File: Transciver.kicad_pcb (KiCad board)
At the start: 2 copper layers, 4 parts, among them SW1 SW_DIP_x02

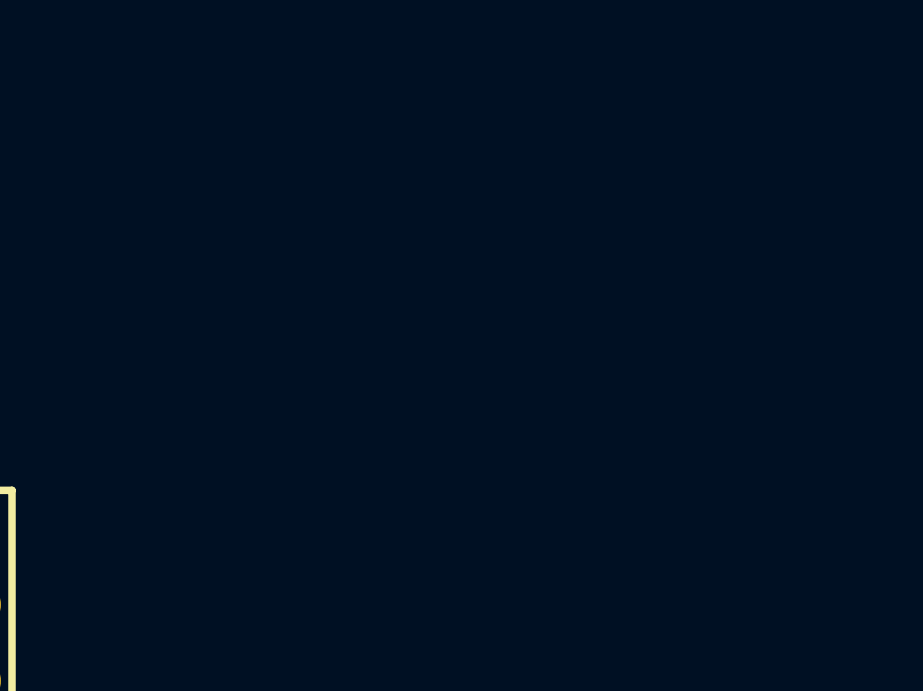
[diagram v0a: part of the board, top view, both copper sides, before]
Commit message: Debug Led and Resistor added
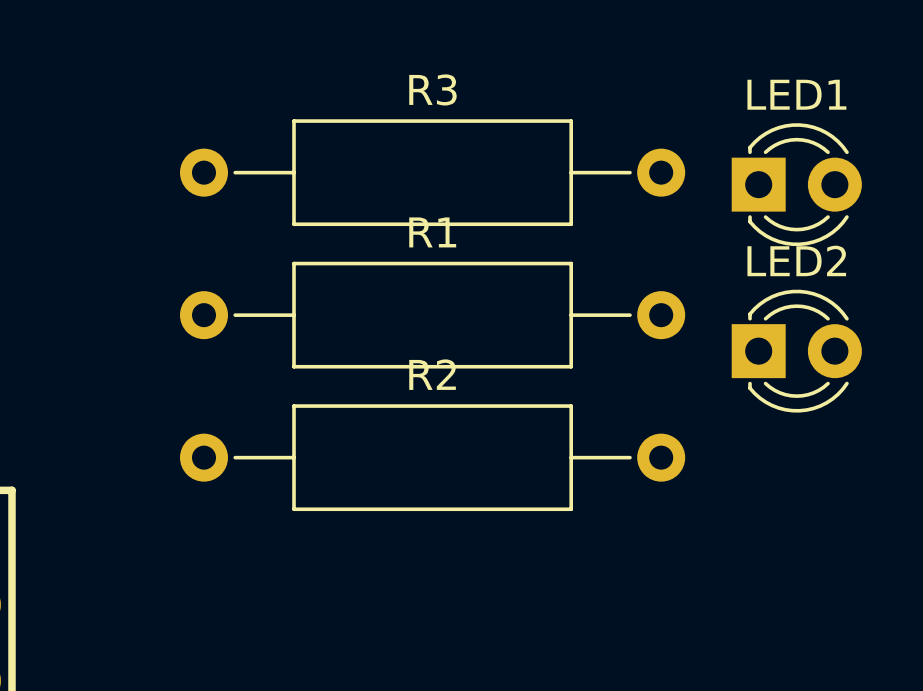
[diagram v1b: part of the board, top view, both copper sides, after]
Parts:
- added LED1: LED, LED_THT:LED_D3.0mm, F.Cu at (121.2, 31.8)
- added LED2: LED, LED_THT:LED_D3.0mm, F.Cu at (121.2, 37.4)
- added R1: 220K, Resistor_THT:R_Axial_DIN0309_L9.0mm_D3.2mm_P15.24mm_Horizontal, F.Cu at (102.7, 36.1)
- added R2: 10K, Resistor_THT:R_Axial_DIN0309_L9.0mm_D3.2mm_P15.24mm_Horizontal, F.Cu at (102.7, 40.9)
- added R3: 220K, Resistor_THT:R_Axial_DIN0309_L9.0mm_D3.2mm_P15.24mm_Horizontal, F.Cu at (102.7, 31.4)
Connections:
- ArduinoNanoEvery1 pad 14: unconnected-(ArduinoNanoEvery1-Pad14) -> GND
- ArduinoNanoEvery1 pad 22: unconnected-(ArduinoNanoEvery1-Pad22) -> /D4
- SW1 pad 2: GND -> Net-(R2-Pad1)
